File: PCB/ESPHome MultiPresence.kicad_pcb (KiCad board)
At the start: 2 copper layers, 51.7 x 80.7 mm, 48 parts, among them J1 Conn_01x06, J2 Conn_01x03, J3 USB_C_Receptacle_Power, J4 Conn_01x02, SW1 SW_Push, SW2 SW_Push, U1 ESP32-WROOM-32, U2 TLV75533PDBV, U3 SEN0395, U4 SHTC3, U5 SEN0395, U6 TSL2591, U7 EKMC1603113

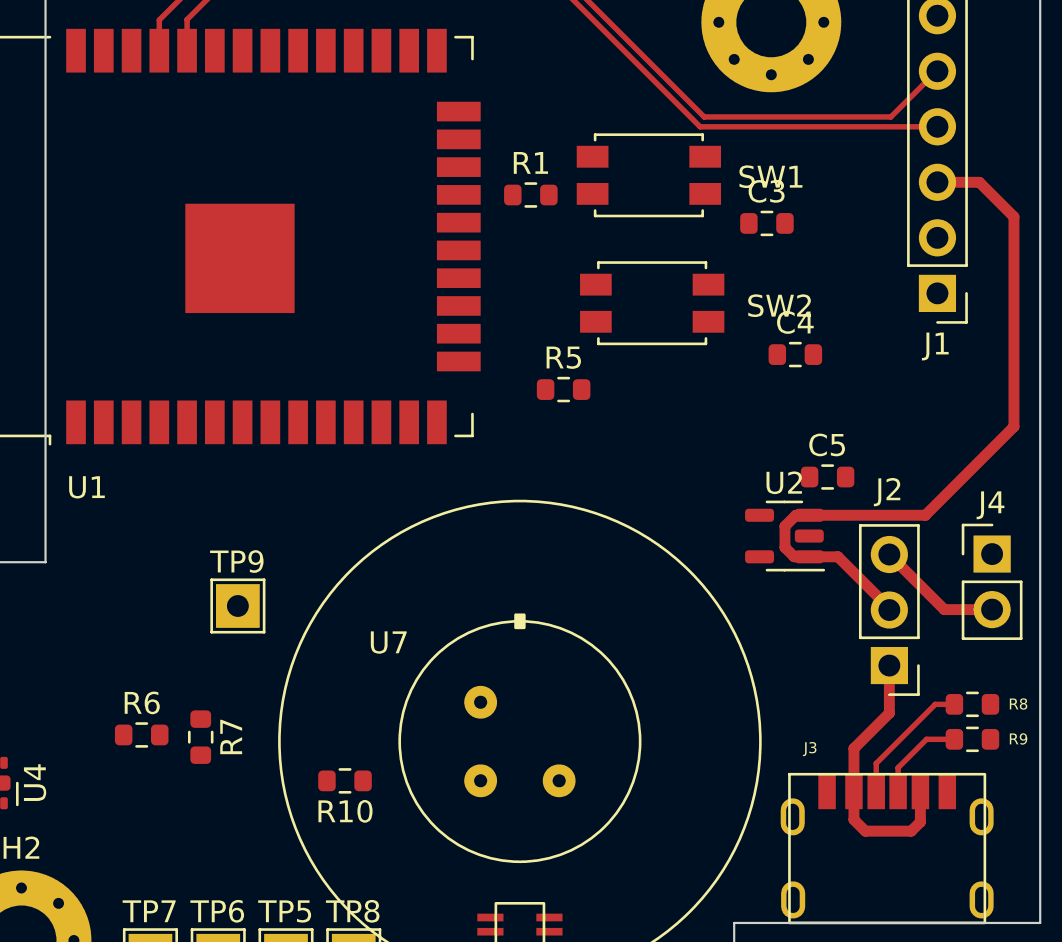
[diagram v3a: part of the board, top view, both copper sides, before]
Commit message: added and laid out what can be a single sidded board for testing
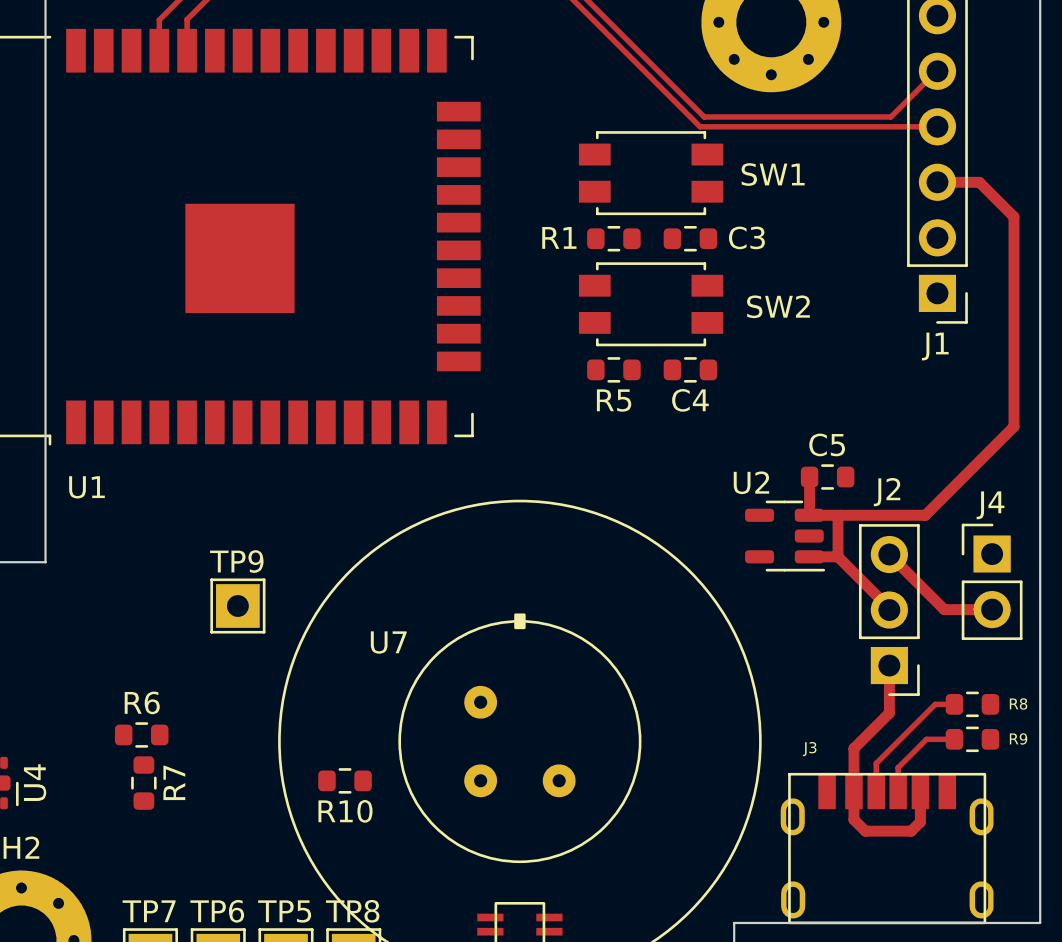
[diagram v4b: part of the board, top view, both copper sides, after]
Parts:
- moved C4 4.85 mm to (237.8, 79.7), turned to 180 degrees
- moved R1 4.29 mm to (234.3, 73.7), turned to 180 degrees
- moved C3 3.57 mm to (237.8, 73.7), turned to 180 degrees
- moved R7 3.34 mm to (212.8, 98.6)
- moved R5 2.47 mm to (234.3, 79.7), turned to 180 degrees
- moved SW1 0.14 mm to (236.0, 70.7)
- moved SW2 0.07 mm to (236.0, 76.7)
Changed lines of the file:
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@@
   )
   (footprint "Button_Switch_SMD:SW_SPST_EVQP2" (layer "F.Cu")
-    (at 236.05 76.65 180)
+    (at 236 76.7 180)
     (descr "Light Touch Switch, https://industrial.panasonic.com/cdbs/www-data/pdf/ATK0000/ATK0000C374.pdf")
     (tags "SMD SMT SPST EVQP2")
@@
   )
   (footprint "Resistor_SMD:R_0603_1608Metric" (layer "F.Cu")
-    (at 241.3 73)
+    (at 237.8 73.7 180)
     (descr "Resistor SMD 0603 (1608 Metric), square (rectangular) end terminal, IPC_7351 nominal, (Body size source: IPC-SM-782 page 72, https://www.pcb-3d.com/wordpress/wp-content/uploads/ipc-sm-782a_amendment_1_and_2.pdf), generated with kicad-footprint-generator")
     (tags "resistor")
@@
     (property "Sheetname" "MCU, Power")
     (attr smd)
-    (fp_text reference "C3" (at 0 -1.43) (layer "F.SilkS")
+    (fp_text reference "C3" (at -2.6 0) (layer "F.SilkS")
       (effects (font (size 1 1) (thickness 0.15)))
     )
@@
     (fp_line (start 0.8 -0.4125) (end 0.8 0.4125) (layer "F.Fab") (width 0.1))
     (fp_line (start -0.8 -0.4125) (end 0.8 -0.4125) (layer "F.Fab") (width 0.1))
-    (pad "1" smd roundrect (at -0.825 0) (size 0.8 0.95) (layers "F.Cu" "F.Paste" "F.Mask") (roundrect_rratio 0.25)
+    (pad "1" smd roundrect (at -0.825 0 180) (size 0.8 0.95) (layers "F.Cu" "F.Paste" "F.Mask") (roundrect_rratio 0.25)
       (net 3 "Net-(C3-Pad1)") (pintype "passive"))
-    (pad "2" smd roundrect (at 0.825 0) (size 0.8 0.95) (layers "F.Cu" "F.Paste" "F.Mask") (roundrect_rratio 0.25)
+    (pad "2" smd roundrect (at 0.825 0 180) (size 0.8 0.95) (layers "F.Cu" "F.Paste" "F.Mask") (roundrect_rratio 0.25)
       (net 2 "GND") (pintype "passive"))
     (model "${KICAD6_3DMODEL_DIR}/Resistor_SMD.3dshapes/R_0603_1608Metric.wrl"
@@
   )
   (footprint "Resistor_SMD:R_0603_1608Metric" (layer "F.Cu")
-    (at 230.5 71.7)
+    (at 234.3 73.7 180)
     (descr "Resistor SMD 0603 (1608 Metric), square (rectangular) end terminal, IPC_7351 nominal, (Body size source: IPC-SM-782 page 72, https://www.pcb-3d.com/wordpress/wp-content/uploads/ipc-sm-782a_amendment_1_and_2.pdf), generated with kicad-footprint-generator")
     (tags "resistor")
@@
     (property "Sheetname" "MCU, Power")
     (attr smd)
-    (fp_text reference "R1" (at 0 -1.43) (layer "F.SilkS")
+    (fp_text reference "R1" (at 2.5 0) (layer "F.SilkS")
       (effects (font (size 1 1) (thickness 0.15)))
     )
@@
     (fp_line (start 0.8 -0.4125) (end 0.8 0.4125) (layer "F.Fab") (width 0.1))
     (fp_line (start -0.8 0.4125) (end -0.8 -0.4125) (layer "F.Fab") (width 0.1))
-    (pad "1" smd roundrect (at -0.825 0) (size 0.8 0.95) (layers "F.Cu" "F.Paste" "F.Mask") (roundrect_rratio 0.25)
+    (pad "1" smd roundrect (at -0.825 0 180) (size 0.8 0.95) (layers "F.Cu" "F.Paste" "F.Mask") (roundrect_rratio 0.25)
       (net 1 "+3.3V") (pintype "passive"))
-    (pad "2" smd roundrect (at 0.825 0) (size 0.8 0.95) (layers "F.Cu" "F.Paste" "F.Mask") (roundrect_rratio 0.25)
+    (pad "2" smd roundrect (at 0.825 0 180) (size 0.8 0.95) (layers "F.Cu" "F.Paste" "F.Mask") (roundrect_rratio 0.25)
       (net 3 "Net-(C3-Pad1)") (pintype "passive"))
     (model "${KICAD6_3DMODEL_DIR}/Resistor_SMD.3dshapes/R_0603_1608Metric.wrl"
@@
   )
   (footprint "Resistor_SMD:R_0603_1608Metric" (layer "F.Cu")
-    (at 232 80.6)
+    (at 234.3 79.7 180)
     (descr "Resistor SMD 0603 (1608 Metric), square (rectangular) end terminal, IPC_7351 nominal, (Body size source: IPC-SM-782 page 72, https://www.pcb-3d.com/wordpress/wp-content/uploads/ipc-sm-782a_amendment_1_and_2.pdf), generated with kicad-footprint-generator")
     (tags "resistor")
@@
     (fp_line (start -0.8 -0.4125) (end 0.8 -0.4125) (layer "F.Fab") (width 0.1))
     (fp_line (start 0.8 0.4125) (end -0.8 0.4125) (layer "F.Fab") (width 0.1))
-    (pad "1" smd roundrect (at -0.825 0) (size 0.8 0.95) (layers "F.Cu" "F.Paste" "F.Mask") (roundrect_rratio 0.25)
+    (pad "1" smd roundrect (at -0.825 0 180) (size 0.8 0.95) (layers "F.Cu" "F.Paste" "F.Mask") (roundrect_rratio 0.25)
       (net 1 "+3.3V") (pintype "passive"))
-    (pad "2" smd roundrect (at 0.825 0) (size 0.8 0.95) (layers "F.Cu" "F.Paste" "F.Mask") (roundrect_rratio 0.25)
+    (pad "2" smd roundrect (at 0.825 0 180) (size 0.8 0.95) (layers "F.Cu" "F.Paste" "F.Mask") (roundrect_rratio 0.25)
       (net 4 "Net-(C4-Pad1)") (pintype "passive"))
     (model "${KICAD6_3DMODEL_DIR}/Resistor_SMD.3dshapes/R_0603_1608Metric.wrl"
@@
   )
   (footprint "Resistor_SMD:R_0603_1608Metric" (layer "F.Cu")
-    (at 242.6 79)
+    (at 237.8 79.7 180)
     (descr "Resistor SMD 0603 (1608 Metric), square (rectangular) end terminal, IPC_7351 nominal, (Body size source: IPC-SM-782 page 72, https://www.pcb-3d.com/wordpress/wp-content/uploads/ipc-sm-782a_amendment_1_and_2.pdf), generated with kicad-footprint-generator")
     (tags "resistor")
@@
     (fp_line (start -0.8 -0.4125) (end 0.8 -0.4125) (layer "F.Fab") (width 0.1))
     (fp_line (start -0.8 0.4125) (end -0.8 -0.4125) (layer "F.Fab") (width 0.1))
-    (pad "1" smd roundrect (at -0.825 0) (size 0.8 0.95) (layers "F.Cu" "F.Paste" "F.Mask") (roundrect_rratio 0.25)
+    (pad "1" smd roundrect (at -0.825 0 180) (size 0.8 0.95) (layers "F.Cu" "F.Paste" "F.Mask") (roundrect_rratio 0.25)
       (net 4 "Net-(C4-Pad1)") (pintype "passive"))
-    (pad "2" smd roundrect (at 0.825 0) (size 0.8 0.95) (layers "F.Cu" "F.Paste" "F.Mask") (roundrect_rratio 0.25)
+    (pad "2" smd roundrect (at 0.825 0 180) (size 0.8 0.95) (layers "F.Cu" "F.Paste" "F.Mask") (roundrect_rratio 0.25)
       (net 2 "GND") (pintype "passive"))
     (model "${KICAD6_3DMODEL_DIR}/Resistor_SMD.3dshapes/R_0603_1608Metric.wrl"
@@
     (property "Sheetname" "MCU, Power")
     (attr smd)
-    (fp_text reference "U2" (at 0 2.4) (layer "F.SilkS")
+    (fp_text reference "U2" (at 1.5 2.4) (layer "F.SilkS")
       (effects (font (size 1 1) (thickness 0.15)))
     )
@@
   )
   (footprint "Resistor_SMD:R_0603_1608Metric" (layer "F.Cu")
-    (at 215.4 96.5 -90)
+    (at 212.8 98.6 -90)
     (descr "Resistor SMD 0603 (1608 Metric), square (rectangular) end terminal, IPC_7351 nominal, (Body size source: IPC-SM-782 page 72, https://www.pcb-3d.com/wordpress/wp-content/uploads/ipc-sm-782a_amendment_1_and_2.pdf), generated with kicad-footprint-generator")
     (tags "resistor")
@@
   )
   (footprint "Button_Switch_SMD:SW_SPST_EVQP2" (layer "F.Cu")
-    (at 235.9 70.8 180)
+    (at 236 70.7 180)
     (descr "Light Touch Switch, https://industrial.panasonic.com/cdbs/www-data/pdf/ATK0000/ATK0000C374.pdf")
     (tags "SMD SMT SPST EVQP2")
@@
   (gr_line (start 246.8 100) (end 246.8 110.5) (layer "User.1") (width 0.15))
   (segment (start 246.9 90.6) (end 246.9 90.685) (width 0.5) (layer "F.Cu") (net 5))
-  (segment (start 242.125 87.825) (end 242.55 88.25) (width 0.5) (layer "F.Cu") (net 5))
   (segment (start 252.6 72.7) (end 252.6 82.3) (width 0.5) (layer "F.Cu") (net 5))
+  (segment (start 244.55 86.45) (end 244.65 86.35) (width 0.5) (layer "F.Cu") (net 5))
   (segment (start 252.6 82.3) (end 248.55 86.35) (width 0.5) (layer "F.Cu") (net 5))
   (segment (start 243.2375 88.25) (end 244.55 88.25) (width 0.5) (layer "F.Cu") (net 5))
   (segment (start 206.2 112.9) (end 206.2 112.8) (width 0.8) (layer "F.Cu") (net 5))
-  (segment (start 242.55 88.25) (end 243.2375 88.25) (width 0.5) (layer "F.Cu") (net 5))
   (segment (start 204.3 124.68) (end 209.97 130.35) (width 0.8) (layer "F.Cu") (net 5))
+  (segment (start 244.65 86.35) (end 243.2375 86.35) (width 0.5) (layer "F.Cu") (net 5))
   (segment (start 216.35 111.27) (end 207.83 111.27) (width 0.8) (layer "F.Cu") (net 5))
-  (segment (start 242.625 86.35) (end 242.125 86.85) (width 0.5) (layer "F.Cu") (net 5))
+  (segment (start 244.55 88.25) (end 244.55 86.45) (width 0.5) (layer "F.Cu") (net 5))
   (segment (start 249.1 71.12) (end 251.02 71.12) (width 0.5) (layer "F.Cu") (net 5))
-  (segment (start 248.55 86.35) (end 243.2375 86.35) (width 0.5) (layer "F.Cu") (net 5))
-  (segment (start 243.2375 86.35) (end 242.625 86.35) (width 0.5) (layer "F.Cu") (net 5))
-  (segment (start 242.125 86.85) (end 242.125 87.825) (width 0.5) (layer "F.Cu") (net 5))
+  (segment (start 243.25 84.6) (end 243.25 86.3375) (width 0.5) (layer "F.Cu") (net 5))
+  (segment (start 248.55 86.35) (end 244.65 86.35) (width 0.5) (layer "F.Cu") (net 5))
+  (segment (start 243.25 86.3375) (end 243.2375 86.35) (width 0.5) (layer "F.Cu") (net 5))
   (segment (start 206.3 112.8) (end 206.2 112.8) (width 0.8) (layer "F.Cu") (net 5))
   (segment (start 251.02 71.12) (end 252.6 72.7) (width 0.5) (layer "F.Cu") (net 5))
